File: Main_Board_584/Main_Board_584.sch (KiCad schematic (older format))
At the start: 77 parts, among them J1 Conn_02x05_Top_Bottom, J2 USB_OTG, J3 Micro_SD_Card, J4 Edge_SMA, J5 Conn_01x02, J6 Conn_01x02, J7 Conn_01x02, M1 M3, M2 M3, M3 M3, M4 M3, M5 M3, Q1 Q_NJFET_GDS, U1 SAMD21G18A, U2 LMZ21701, U3 TMP36, U4 MS5607, U5 HDC1080, U6 RFM23BP, U7 MPU9250, U8 UltimateGPS, Y1 Crystal

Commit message: Remembered to add chip identifier
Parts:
- gave numbers to parts that had none: 1
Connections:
- net at R14.1: now also J7.1 (Pin_1), U9.3 (VIN+)

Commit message: Added Reference
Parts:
- added C?: 1uF, Capacitors_SMD:C_0603, symbol C
- added C?: 2.2uF, Capacitors_SMD:C_0603, symbol C
- added U?: LT1461, symbol LT1461
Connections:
- net 2V5: now also C?.1, U?.6 (VOUT)
- net GND: now also C?.2, C?.2, U?.4 (GND)
- net VIN: now also C?.1, U?.2 (VIN), U?.3 (nSHDN)
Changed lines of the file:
@@
 LIBS:valves
 LIBS:SPACE_584
-LIBS:dk_Linear-Amplifiers-Instrumentation-OP-Amps-Buffer-Amps
-LIBS:dk_Linear-Amplifiers-Audio
+LIBS:live_telem
 LIBS:Main_Board_584-cache
 EELAYER 25 0
@@
 	5650 9450 5550 9450
 Wire Wire Line
-	5550 9350 5550 9450
+	5550 9450 5550 9350
 Wire Wire Line
 	4750 9350 5650 9350
@@
 	12700 3250 12700 3300
 Wire Wire Line
-	12400 3650 12800 3650
+	12400 3650 12850 3650
 Wire Wire Line
 	12700 3650 12700 3600
@@
 	2150 6150 2200 6150
 Connection ~ 2200 6150
-Wire Wire Line
-	13450 3350 12800 3350
-Wire Wire Line
-	12800 3350 12800 3650
 Connection ~ 12700 3650
 Wire Wire Line
@@
 Wire Wire Line
 	14600 8700 14600 8450
-Wire Wire Line
-	13300 7850 13300 7850
-Wire Wire Line
-	13300 7700 13300 8100
 Connection ~ 13300 7700
 Wire Wire Line
@@
 Connection ~ 13300 8700
 Connection ~ 15450 8250
+Wire Wire Line
+	13300 8100 13300 7700
+$Comp
+L LT1461 U?
+U 1 1 5A703EA6
+P 9000 6750
+F 0 "U?" H 9050 6800 60  0000 C CNN
+F 1 "LT1461" H 9150 6400 60  0000 C CNN
+F 2 "" H 9000 6750 60  0001 C CNN
+F 3 "" H 9000 6750 60  0001 C CNN
+	1    9000 6750
+	1    0    0    -1
+$EndComp
+Text GLabel 8050 6850 0    60   Input ~ 0
+VIN
+$Comp
+L C C?
+U 1 1 5A705189
+P 8150 7050
+F 0 "C?" H 8175 7150 50  0000 L CNN
+F 1 "1uF" H 8175 6950 50  0000 L CNN
+F 2 "Capacitors_SMD:C_0603" H 8188 6900 50  0001 C CNN
+F 3 "" H 8150 7050 50  0001 C CNN
+	1    8150 7050
+	1    0    0    -1
+$EndComp
+$Comp
+L C C?
+U 1 1 5A705360
+P 10500 7050
+F 0 "C?" H 10525 7150 50  0000 L CNN
+F 1 "2.2uF" H 10525 6950 50  0000 L CNN
+F 2 "Capacitors_SMD:C_0603" H 10538 6900 50  0001 C CNN
+F 3 "" H 10500 7050 50  0001 C CNN
+	1    10500 7050
+	1    0    0    -1
+$EndComp
+Wire Wire Line
+	8150 6900 8150 6850
+Wire Wire Line
+	8050 6850 8800 6850
+Connection ~ 8150 6850
+Wire Wire Line
+	8800 6950 8700 6950
+Wire Wire Line
+	8700 6950 8700 6850
+Connection ~ 8700 6850
+Wire Wire Line
+	8150 7200 8150 7250
+Wire Wire Line
+	8150 7250 10850 7250
+Wire Wire Line
+	9850 7250 9850 6950
+Wire Wire Line
+	9850 6950 9800 6950
+Wire Wire Line
+	10500 7250 10500 7200
+Connection ~ 9850 7250
+Text GLabel 10850 7250 2    60   Input ~ 0
+GND
+Connection ~ 10500 7250
+Wire Wire Line
+	10500 6900 10500 6850
+Wire Wire Line
+	9800 6850 10850 6850
+Text GLabel 10850 6850 2    60   Input ~ 0
+2V5
+Connection ~ 10500 6850
+Wire Wire Line
+	12850 3650 12850 3350
+Wire Wire Line
+	12850 3350 13450 3350
 $EndSCHEMATC

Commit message: Added Test Points
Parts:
- added J? (x3): Conn_01x02, MASA:A33199CT-ND, symbol Conn_01x02
- added Q?: Q_NJFET_GDS, TO_SOT_Packages_THT:TO-220-3_Vertical, symbol Q_NJFET_GDS
- added R? (x2): 0, Capacitors_SMD:C_0603, symbol R
- added R?: 330, Capacitors_SMD:C_0603, symbol R
- added TP? (x20): TEST, symbol TEST
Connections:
- net 2V5: now also TP?.1, TP?.1
- net BARO_CS: now also TP?.1
- net FTU_FIRE: now also R?.2; no longer Q1.1 (G)
- net GND: now also J?.1 (Pin_1), J?.1 (Pin_1), Q?.3 (S), TP?.1
- net MISO: now also TP?.1
- net MOSI: now also TP?.1
- net MPU_CS: now also TP?.1
- net RADIO_CS: now also TP?.1
- net RX: now also R?.1; no longer U8.5 (TX)
- net SCL: now also TP?.1
- net SCLK: now also TP?.1
- net SDA: now also TP?.1
- net THERM: now also TP?.1
- net TMP_VOUT: now also TP?.1
- net TMP_nSHDN: now also TP?.1
- net TX: now also R?.1; no longer U8.6 (RX)
- net VIN: now also J?.2 (Pin_2), TP?.1
- net uSD_CS: now also TP?.1
- new net: Q1.1 (G), R?.1, TP?.1
- new net: R?.2, TP?.1, U8.5 (TX)
- new net: R?.2, TP?.1, U8.6 (RX)
- new net: J?.1 (Pin_1), Q?.2 (D)
- new net AIN_1: J?.2 (Pin_2)
- new net AIN_2: J?.2 (Pin_2)
- new net HEAT_ON: Q?.1 (G), TP?.1
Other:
- note added: "General Input 1"
- note added: "General Input 2\n"
- note added: "Heater"
- moved on the sheet: BT1, BT2, C?, J5, J6, M1, M2, M3, M4, M5, Q1, R15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

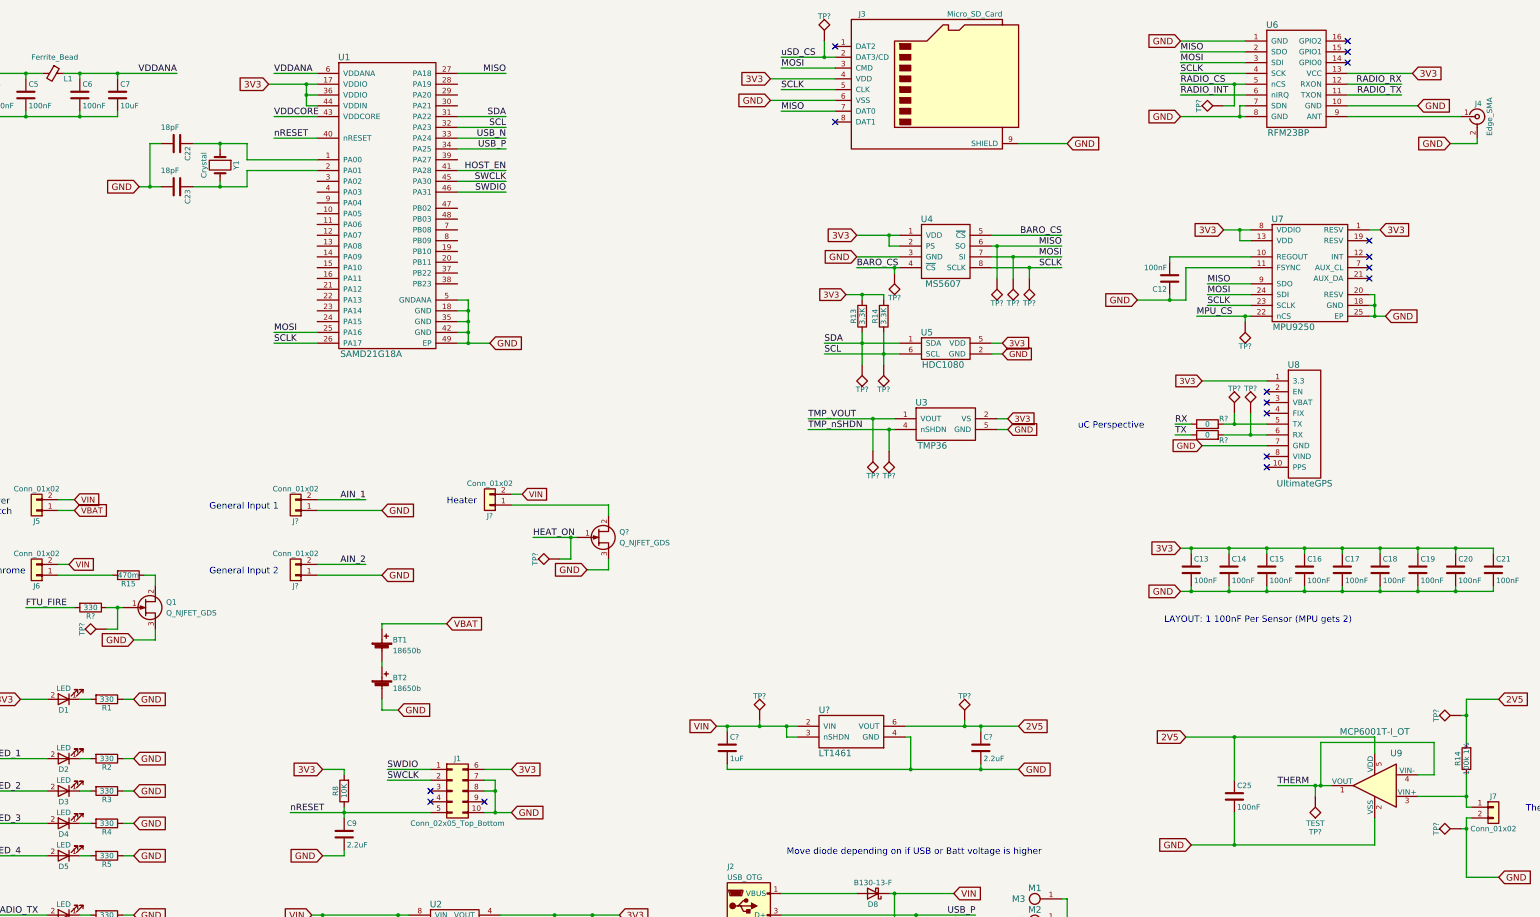
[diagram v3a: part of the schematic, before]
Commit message: Added Footprint Associations
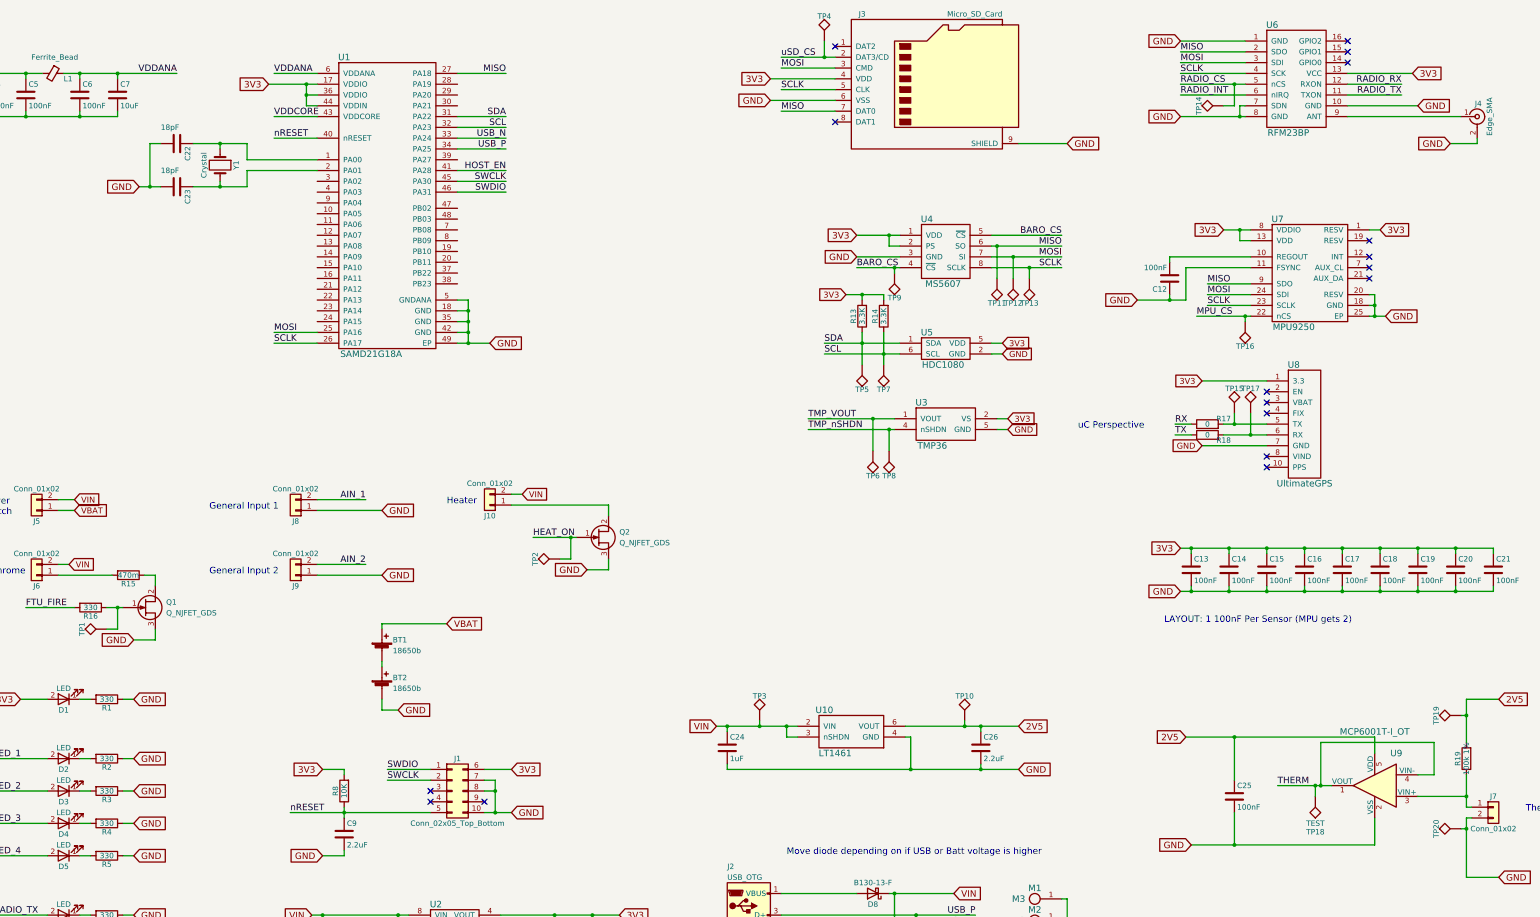
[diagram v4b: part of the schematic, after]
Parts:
- TP1, TP10, TP11, TP12, TP13, TP14, TP15, TP16, TP17, TP18, TP19, TP2, TP20, TP3, TP4, TP5, TP6, TP7, TP8, TP9: renamed from TP?; footprint (none) -> MASA:0603_TP
- U10: renamed from U?; footprint (none) -> Housings_SOIC:SOIC-8_3.9x4.9mm_Pitch1.27mm
- gave numbers to parts that had none: 9
- renumbered R14 to R19
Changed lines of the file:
@@
 GND
 $Comp
-L R R14
+L R R19
 U 1 1 5A6E74E1
 P 15450 7900
-F 0 "R14" V 15530 7900 50  0000 C CNN
+F 0 "R19" V 15530 7900 50  0000 C CNN
 F 1 "100k 1%" V 15450 7900 50  0000 C CNN
 F 2 "Capacitors_SMD:C_0603" V 15380 7900 50  0001 C CNN
@@
 	13300 8100 13300 7700
 $Comp
-L LT1461 U?
+L LT1461 U10
 U 1 1 5A703EA6
 P 9450 7500
-F 0 "U?" H 9500 7550 60  0000 C CNN
+F 0 "U10" H 9500 7550 60  0000 C CNN
 F 1 "LT1461" H 9600 7150 60  0000 C CNN
-F 2 "" H 9450 7500 60  0001 C CNN
+F 2 "Housings_SOIC:SOIC-8_3.9x4.9mm_Pitch1.27mm" H 9450 7500 60  0001 C CNN
 F 3 "" H 9450 7500 60  0001 C CNN
 	1    9450 7500
@@
 VIN
 $Comp
-L C C?
+L C C24
 U 1 1 5A705189
 P 8600 7800
-F 0 "C?" H 8625 7900 50  0000 L CNN
+F 0 "C24" H 8625 7900 50  0000 L CNN
 F 1 "1uF" H 8625 7700 50  0000 L CNN
 F 2 "Capacitors_SMD:C_0603" H 8638 7650 50  0001 C CNN
@@
 $EndComp
 $Comp
-L C C?
+L C C26
 U 1 1 5A705360
 P 10950 7800
-F 0 "C?" H 10975 7900 50  0000 L CNN
+F 0 "C26" H 10975 7900 50  0000 L CNN
 F 1 "2.2uF" H 10975 7700 50  0000 L CNN
 F 2 "Capacitors_SMD:C_0603" H 10988 7650 50  0001 C CNN
@@
 Connection ~ 2950 6500
 $Comp
-L TEST TP?
+L TEST TP18
 U 1 1 5A70FC9E
 P 14050 8250
-F 0 "TP?" H 14050 8550 50  0000 C BNN
+F 0 "TP18" H 14050 8550 50  0000 C BNN
 F 1 "TEST" H 14050 8500 50  0000 C CNN
-F 2 "" H 14050 8250 50  0001 C CNN
+F 2 "MASA:0603_TP" H 14050 8250 50  0001 C CNN
 F 3 "" H 14050 8250 50  0001 C CNN
 	1    14050 8250
@@
 	15400 7500 15450 7500
 $Comp
-L TEST TP?
+L TEST TP6
 U 1 1 5A712065
 P 9950 5050
-F 0 "TP?" H 9950 5250 50  0000 C BNN
+F 0 "TP6" H 9950 5250 50  0000 C BNN
 F 1 "TEST" H 9950 5300 50  0001 C CNN
-F 2 "" H 9950 5050 50  0001 C CNN
+F 2 "MASA:0603_TP" H 9950 5050 50  0001 C CNN
 F 3 "" H 9950 5050 50  0001 C CNN
 	1    9950 5050
@@
 $EndComp
 $Comp
-L TEST TP?
+L TEST TP10
 U 1 1 5A713AE1
 P 10800 7550
-F 0 "TP?" H 10800 7750 50  0000 C BNN
+F 0 "TP10" H 10800 7750 50  0000 C BNN
 F 1 "TEST" H 10800 7800 50  0001 C CNN
-F 2 "" H 10800 7550 50  0001 C CNN
+F 2 "MASA:0603_TP" H 10800 7550 50  0001 C CNN
 F 3 "" H 10800 7550 50  0001 C CNN
 	1    10800 7550
@@
 $EndComp
 $Comp
-L TEST TP?
+L TEST TP3
 U 1 1 5A713C27
 P 8900 7550
-F 0 "TP?" H 8900 7750 50  0000 C BNN
+F 0 "TP3" H 8900 7750 50  0000 C BNN
 F 1 "TEST" H 8900 7800 50  0001 C CNN
-F 2 "" H 8900 7550 50  0001 C CNN
+F 2 "MASA:0603_TP" H 8900 7550 50  0001 C CNN
 F 3 "" H 8900 7550 50  0001 C CNN
 	1    8900 7550
@@
 $EndComp
 $Comp
-L TEST TP?
+L TEST TP19
 U 1 1 5A71433D
 P 15400 7500
-F 0 "TP?" H 15400 7700 50  0000 C BNN
+F 0 "TP19" H 15400 7700 50  0000 C BNN
 F 1 "TEST" H 15400 7750 50  0001 C CNN
-F 2 "" H 15400 7500 50  0001 C CNN
+F 2 "MASA:0603_TP" H 15400 7500 50  0001 C CNN
 F 3 "" H 15400 7500 50  0001 C CNN
 	1    15400 7500
@@
 $EndComp
 $Comp
-L TEST TP?
+L TEST TP20
 U 1 1 5A7145C8
 P 15400 8550
-F 0 "TP?" H 15400 8750 50  0000 C BNN
+F 0 "TP20" H 15400 8750 50  0000 C BNN
 F 1 "TEST" H 15400 8800 50  0001 C CNN
-F 2 "" H 15400 8550 50  0001 C CNN
+F 2 "MASA:0603_TP" H 15400 8550 50  0001 C CNN
 F 3 "" H 15400 8550 50  0001 C CNN
 	1    15400 8550
@@
 $EndComp
 $Comp
-L TEST TP?
+L TEST TP1
 U 1 1 5A716FCC
 P 2850 6700
-F 0 "TP?" H 2850 6900 50  0000 C BNN
+F 0 "TP1" H 2850 6900 50  0000 C BNN
 F 1 "TEST" H 2850 6950 50  0001 C CNN
-F 2 "" H 2850 6700 50  0001 C CNN
+F 2 "MASA:0603_TP" H 2850 6700 50  0001 C CNN
 F 3 "" H 2850 6700 50  0001 C CNN
 	1    2850 6700
@@
 $EndComp
 $Comp
-L TEST TP?
+L TEST TP8
 U 1 1 5A718415
 P 10100 5050
-F 0 "TP?" H 10100 5250 50  0000 C BNN
+F 0 "TP8" H 10100 5250 50  0000 C BNN
 F 1 "TEST" H 10100 5300 50  0001 C CNN
-F 2 "" H 10100 5050 50  0001 C CNN
+F 2 "MASA:0603_TP" H 10100 5050 50  0001 C CNN
 F 3 "" H 10100 5050 50  0001 C CNN
 	1    10100 5050
@@
 Connection ~ 9950 4750
 $Comp
-L TEST TP?
+L TEST TP7
 U 1 1 5A719B55
 P 10050 4250
-F 0 "TP?" H 10050 4450 50  0000 C BNN
+F 0 "TP7" H 10050 4450 50  0000 C BNN
 F 1 "TEST" H 10050 4500 50  0001 C CNN
-F 2 "" H 10050 4250 50  0001 C CNN
+F 2 "MASA:0603_TP" H 10050 4250 50  0001 C CNN
 F 3 "" H 10050 4250 50  0001 C CNN
 	1    10050 4250
@@
 $EndComp
 $Comp
-L TEST TP?
+L TEST TP5
 U 1 1 5A719C7E
 P 9850 4250
-F 0 "TP?" H 9850 4450 50  0000 C BNN
+F 0 "TP5" H 9850 4450 50  0000 C BNN
 F 1 "TEST" H 9850 4500 50  0001 C CNN
-F 2 "" H 9850 4250 50  0001 C CNN
+F 2 "MASA:0603_TP" H 9850 4250 50  0001 C CNN
 F 3 "" H 9850 4250 50  0001 C CNN
 	1    9850 4250
@@
 $EndComp
 $Comp
-L TEST TP?
+L TEST TP9
 U 1 1 5A71A5B8
 P 10150 3400
-F 0 "TP?" H 10150 3600 50  0000 C BNN
+F 0 "TP9" H 10150 3600 50  0000 C BNN
 F 1 "TEST" H 10150 3650 50  0001 C CNN
-F 2 "" H 10150 3400 50  0001 C CNN
+F 2 "MASA:0603_TP" H 10150 3400 50  0001 C CNN
 F 3 "" H 10150 3400 50  0001 C CNN
 	1    10150 3400
@@
 Connection ~ 10150 3350
 $Comp
-L TEST TP?
+L TEST TP11
 U 1 1 5A71AF7B
 P 11100 3450
-F 0 "TP?" H 11100 3650 50  0000 C BNN
+F 0 "TP11" H 11100 3650 50  0000 C BNN
 F 1 "TEST" H 11100 3700 50  0001 C CNN
-F 2 "" H 11100 3450 50  0001 C CNN
+F 2 "MASA:0603_TP" H 11100 3450 50  0001 C CNN
 F 3 "" H 11100 3450 50  0001 C CNN
 	1    11100 3450
@@
 $EndComp
 $Comp
-L TEST TP?
+L TEST TP12
 U 1 1 5A71B0B7
 P 11250 3450
-F 0 "TP?" H 11250 3650 50  0000 C BNN
+F 0 "TP12" H 11250 3650 50  0000 C BNN
 F 1 "TEST" H 11250 3700 50  0001 C CNN
-F 2 "" H 11250 3450 50  0001 C CNN
+F 2 "MASA:0603_TP" H 11250 3450 50  0001 C CNN
 F 3 "" H 11250 3450 50  0001 C CNN
 	1    11250 3450
@@
 $EndComp
 $Comp
-L TEST TP?
+L TEST TP13
 U 1 1 5A71B1E0
 P 11400 3450
-F 0 "TP?" H 11400 3650 50  0000 C BNN
+F 0 "TP13" H 11400 3650 50  0000 C BNN
 F 1 "TEST" H 11400 3700 50  0001 C CNN
-F 2 "" H 11400 3450 50  0001 C CNN
+F 2 "MASA:0603_TP" H 11400 3450 50  0001 C CNN
 F 3 "" H 11400 3450 50  0001 C CNN
 	1    11400 3450
@@
 Connection ~ 11100 3150
 $Comp
-L TEST TP?
+L TEST TP16
 U 1 1 5A71C928
 P 13400 3850
-F 0 "TP?" H 13400 4050 50  0000 C BNN
+F 0 "TP16" H 13400 4050 50  0000 C BNN
 F 1 "TEST" H 13400 4100 50  0001 C CNN
-F 2 "" H 13400 3850 50  0001 C CNN
+F 2 "MASA:0603_TP" H 13400 3850 50  0001 C CNN
 F 3 "" H 13400 3850 50  0001 C CNN
 	1    13400 3850
@@
 Connection ~ 13400 3800
 $Comp
-L TEST TP?
+L TEST TP14
 U 1 1 5A71D91C
 P 13200 1850
-F 0 "TP?" H 13200 2050 50  0000 C BNN
+F 0 "TP14" H 13200 2050 50  0000 C BNN
 F 1 "TEST" H 13200 2100 50  0001 C CNN
-F 2 "" H 13200 1850 50  0001 C CNN
+F 2 "MASA:0603_TP" H 13200 1850 50  0001 C CNN
 F 3 "" H 13200 1850 50  0001 C CNN
 	1    13200 1850
@@
 Connection ~ 13300 1650
 $Comp
-L TEST TP?
+L TEST TP4
 U 1 1 5A71F059
 P 9500 1250
-F 0 "TP?" H 9500 1450 50  0000 C BNN
+F 0 "TP4" H 9500 1450 50  0000 C BNN
 F 1 "TEST" H 9500 1500 50  0001 C CNN
-F 2 "" H 9500 1250 50  0001 C CNN
+F 2 "MASA:0603_TP" H 9500 1250 50  0001 C CNN
 F 3 "" H 9500 1250 50  0001 C CNN
 	1    9500 1250
@@
 Connection ~ 9500 1400
 $Comp
-L TEST TP?
+L TEST TP15
 U 1 1 5A72133D
 P 13300 4700
-F 0 "TP?" H 13300 4900 50  0000 C BNN
+F 0 "TP15" H 13300 4900 50  0000 C BNN
 F 1 "TEST" H 13300 4950 50  0001 C CNN
-F 2 "" H 13300 4700 50  0001 C CNN
+F 2 "MASA:0603_TP" H 13300 4700 50  0001 C CNN
 F 3 "" H 13300 4700 50  0001 C CNN
 	1    13300 4700
@@
 $EndComp
 $Comp
-L TEST TP?
+L TEST TP17
 U 1 1 5A7217A7
 P 13450 4700
-F 0 "TP?" H 13450 4900 50  0000 C BNN
+F 0 "TP17" H 13450 4900 50  0000 C BNN
 F 1 "TEST" H 13450 4950 50  0001 C CNN
-F 2 "" H 13450 4700 50  0001 C CNN
+F 2 "MASA:0603_TP" H 13450 4700 50  0001 C CNN
 F 3 "" H 13450 4700 50  0001 C CNN
 	1    13450 4700
@@
 Connection ~ 13300 4800
 $Comp
-L R R?
+L R R17
 U 1 1 5A722F49
 P 13050 4800
-F 0 "R?" V 13100 4650 50  0000 C CNN
+F 0 "R17" V 13100 4650 50  0000 C CNN
 F 1 "0" V 13050 4800 50  0000 C CNN
 F 2 "Capacitors_SMD:C_0603" V 12980 4800 50  0001 C CNN
@@
 $EndComp
 $Comp
-L R R?
+L R R18
 U 1 1 5A723C46
 P 13050 4900
-F 0 "R?" V 13000 4750 50  0000 C CNN
+F 0 "R18" V 13000 4750 50  0000 C CNN
 F 1 "0" V 13050 4900 50  0000 C CNN
 F 2 "Capacitors_SMD:C_0603" V 12980 4900 50  0001 C CNN
@@
 	12900 4900 12750 4900
 $Comp
-L Conn_01x02 J?
+L Conn_01x02 J8
 U 1 1 5A72C448
 P 4600 5600
-F 0 "J?" H 4600 5700 50  0000 C CNN
+F 0 "J8" H 4600 5700 50  0000 C CNN
 F 1 "Conn_01x02" H 4600 5400 50  0000 C CNN
 F 2 "MASA:A33199CT-ND" H 4600 5600 50  0001 C CNN
@@
 AIN_1
 $Comp
-L Conn_01x02 J?
+L Conn_01x02 J9
 U 1 1 5A72F09A
 P 4600 6200
-F 0 "J?" H 4600 6300 50  0000 C CNN
+F 0 "J9" H 4600 6300 50  0000 C CNN
 F 1 "Conn_01x02" H 4600 6000 50  0000 C CNN
 F 2 "MASA:A33199CT-ND" H 4600 6200 50  0001 C CNN
@@
 General Input 2\n
 $Comp
-L Conn_01x02 J?
+L Conn_01x02 J10
 U 1 1 5A734687
 P 6400 5550
-F 0 "J?" H 6400 5650 50  0000 C CNN
+F 0 "J10" H 6400 5650 50  0000 C CNN
 F 1 "Conn_01x02" H 6400 5350 50  0000 C CNN
 F 2 "MASA:A33199CT-ND" H 6400 5550 50  0001 C CNN
@@
 VIN
 $Comp
-L Q_NJFET_GDS Q?
+L Q_NJFET_GDS Q2
 U 1 1 5A734695
 P 7400 5850
-F 0 "Q?" H 7600 5900 50  0000 L CNN
+F 0 "Q2" H 7600 5900 50  0000 L CNN
 F 1 "Q_NJFET_GDS" H 7600 5800 50  0000 L CNN
 F 2 "TO_SOT_Packages_THT:TO-220-3_Vertical" H 7600 5950 50  0001 C CNN
@@
 Connection ~ 7150 5850
 $Comp
-L TEST TP?
+L TEST TP2
 U 1 1 5A7346A7
 P 7050 6050
-F 0 "TP?" H 7050 6250 50  0000 C BNN
+F 0 "TP2" H 7050 6250 50  0000 C BNN
 F 1 "TEST" H 7050 6300 50  0001 C CNN
-F 2 "" H 7050 6050 50  0001 C CNN
+F 2 "MASA:0603_TP" H 7050 6050 50  0001 C CNN
 F 3 "" H 7050 6050 50  0001 C CNN
 	1    7050 6050
@@
 $EndComp
 $Comp
-L R R?
+L R R16
 U 1 1 5A738E3C
 P 2700 6500
-F 0 "R?" V 2780 6500 50  0000 C CNN
+F 0 "R16" V 2780 6500 50  0000 C CNN
 F 1 "330" V 2700 6500 50  0000 C CNN
 F 2 "Capacitors_SMD:C_0603" V 2630 6500 50  0001 C CNN
